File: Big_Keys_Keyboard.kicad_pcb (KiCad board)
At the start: 2 copper layers, 100 x 134.5 mm, 9 parts, among them U1 MX1A-11NN, U2 MX1A-11NN, U3 MX1A-11NN, U4 MX1A-11NN

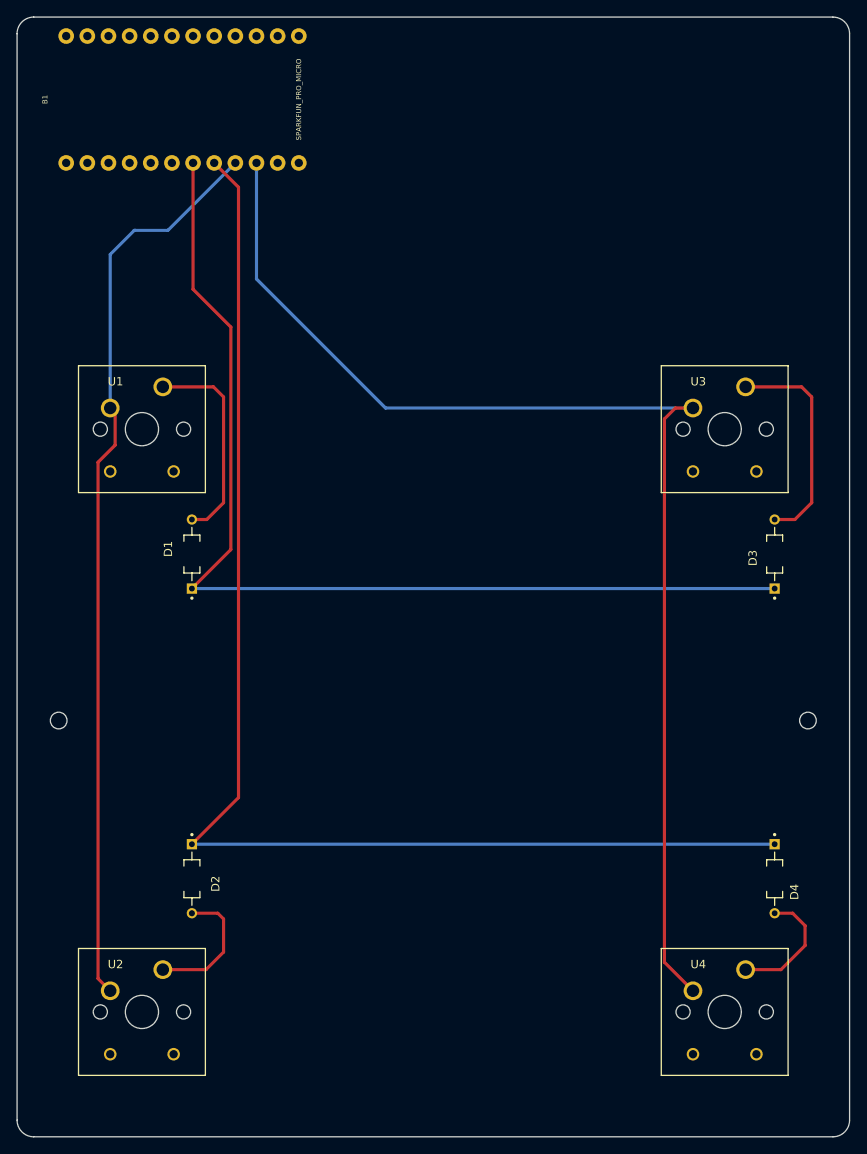
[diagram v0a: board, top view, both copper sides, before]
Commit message: track width changed to 0.5mm and zones filled with ground net
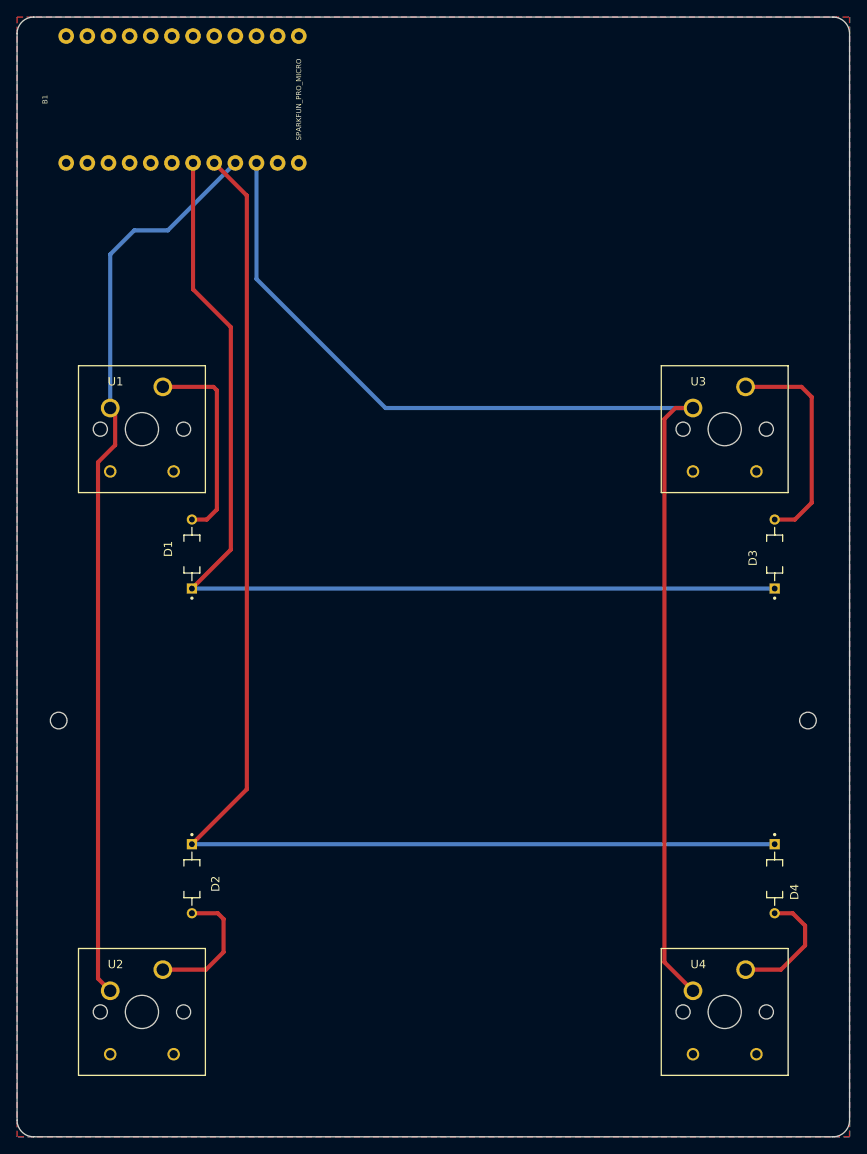
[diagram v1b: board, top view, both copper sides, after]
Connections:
- B1 pad 23: unconnected-(B1-Pad23) -> GND
- B1 pad 3: unconnected-(B1-Pad3) -> GND
- B1 pad 4: unconnected-(B1-Pad4) -> GND
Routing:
- net ROW2: track 155.4 -> 156.2 mm
- net Net-(D1-PadA): track 25.1 -> 24.5 mm
- added copper zone on B.Cu, net GND
- added copper zone on F.Cu, net GND
